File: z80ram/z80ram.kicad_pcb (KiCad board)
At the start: 2 copper layers, 99.8 x 49.9 mm, 18 parts, among them J1 BUS, J2 BUSEXT, Q1 2N7000, U1 Z80CPU, U2 74HCT574, U3 74LS257, U4 AS6C4008-55PCN, U5 74LS138, U6 DS1302+, Y1 XTAL

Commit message: Add pullup resistors on z80ram board
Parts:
- added RN1: R_Network04, Resistor_THT:R_Array_SIP5, F.Cu at (209.0, 144.8)
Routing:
- net /D7: track 111.9 -> 84.2 mm
- net /BB16: track 28.9 -> 54.3 mm
- net /D6: track 116.5 -> 97.8 mm, vias 0 -> 1
- net VCC: track 203.1 -> 217.3 mm
- net /D1: track 78.5 -> 90.6 mm, vias 2 -> 0
- net /D3: track 109.0 -> 120.5 mm
- net /~RD: track 70.4 -> 78.6 mm, vias 0 -> 1
- net Net-(BT1-Pad1): track 30.4 -> 23.1 mm
- net /D5: track 111.5 -> 104.6 mm, vias 0 -> 1
- net /~WAIT: track 36.1 -> 29.6 mm
- net /D2: track 83.8 -> 89.1 mm, vias 2 -> 1
- net /~INT: track 12.5 -> 17.3 mm, vias 0 -> 1
- net /BA16: track 18.6 -> 23.3 mm, vias 1 -> 0
- net /A14: track 52.2 -> 56.5 mm
- net /~MREQ: track 66.8 -> 62.8 mm, vias 1 -> 2
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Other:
- rule trace_min: 0.2 -> 0

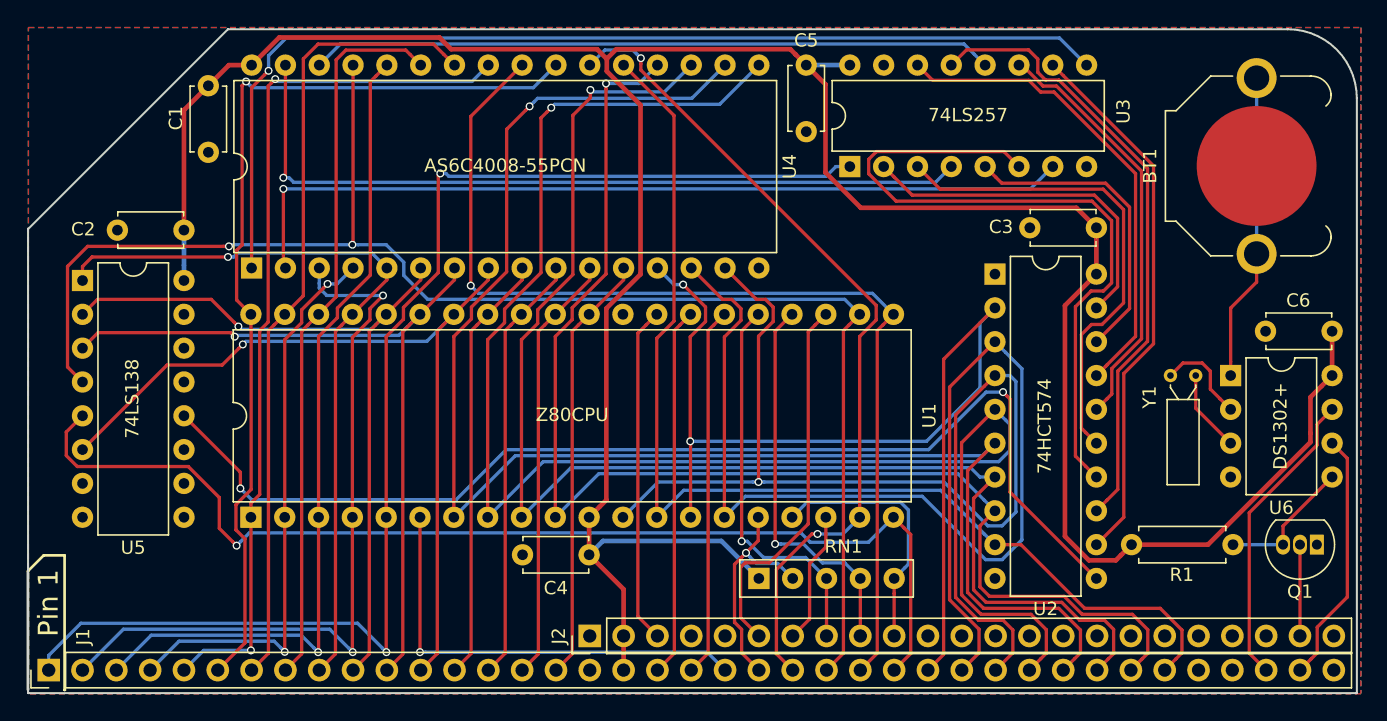
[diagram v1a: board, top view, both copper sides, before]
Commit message: Switch to same capacitor footprint as z80ctrl board
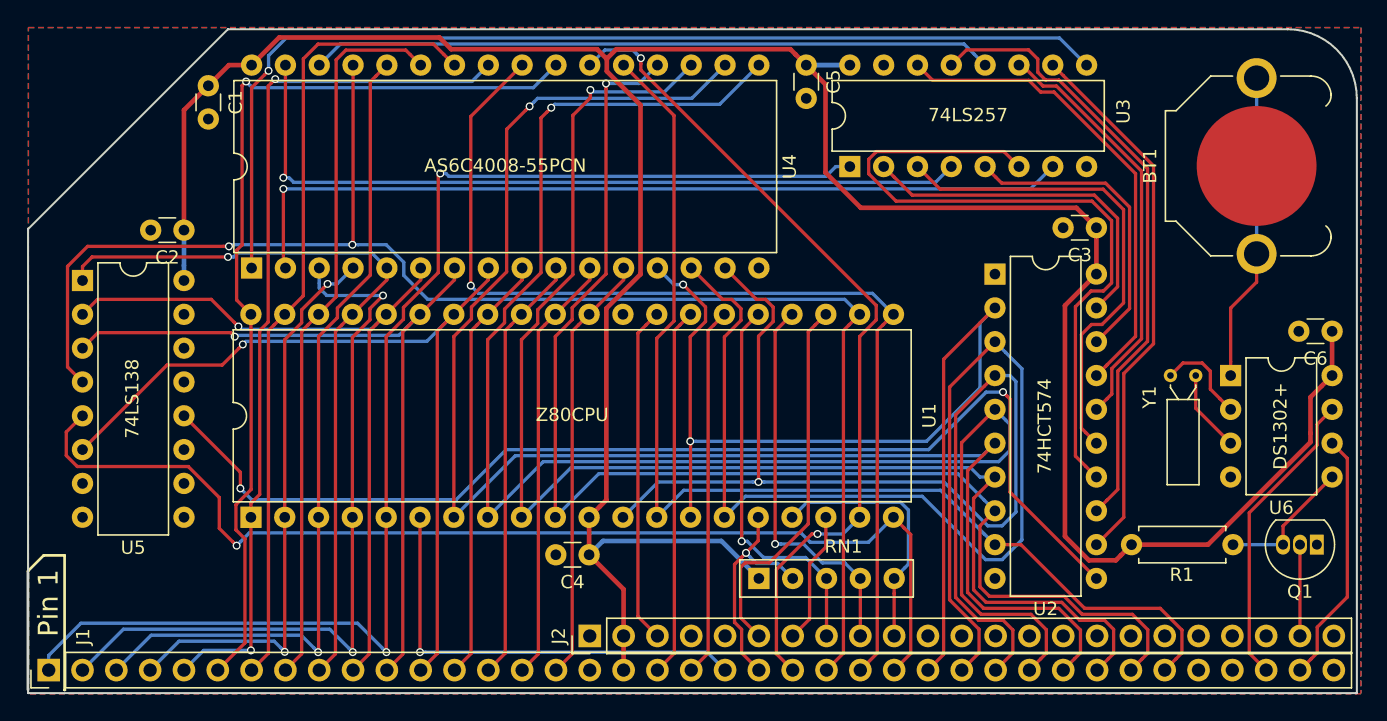
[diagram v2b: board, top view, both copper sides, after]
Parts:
- C1, C2, C3, C4, C5, C6: footprint Capacitor_THT:C_Disc_D4.7mm_W2.5mm_P5.00mm -> Capacitor_THT:C_Disc_D3.0mm_W1.6mm_P2.50mm
- RN1: value R_Network04 -> 10K
